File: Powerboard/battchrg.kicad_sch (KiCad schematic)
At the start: 60 parts, among them IC1 BQ24618RGET-iclr, J1 Thermistor Connection 103AT N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, J5 Conn_01x04_Male, J6 Conn_01x02_Male, J7 IsolationSwitch, Q1 RSJ250P10TL, Q2 RSJ250P10TL, Q3 RSJ250P10TL, Q4 RS1G120MN, Q5 RS1G120MN

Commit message: 3v3 reg cap & inductor changes, added boost capacitor
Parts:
- D1: footprint (none) -> Diode_SMD:D_SOT-23_ANK
- J7: footprint (none) -> Connector_AMASS:AMASS_XT60-M_1x02_P7.20mm_Vertical
- PackLED1, PowerLED1: footprint (none) -> LED_SMD:LED_0603_1608Metric
- TP16, TP17, TP18: footprint (none) -> TestPoint:TestPoint_Pad_D1.0mm
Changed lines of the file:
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@@
       (effects (font (size 1.27 1.27)) (justify left))
     )
-    (property "Footprint" "" (id 2) (at 246.38 96.52 90)
+    (property "Footprint" "Diode_SMD:D_SOT-23_ANK" (id 2) (at 246.38 96.52 90)
       (effects (font (size 1.27 1.27)) hide)
     )
@@
     (property "Reference" "PowerLED1" (id 0) (at 73.66 52.07 90))
     (property "Value" "LED" (id 1) (at 73.66 54.61 90))
-    (property "Footprint" "" (id 2) (at 67.31 53.34 0)
+    (property "Footprint" "LED_SMD:LED_0603_1608Metric" (id 2) (at 67.31 53.34 0)
       (effects (font (size 1.27 1.27)) hide)
     )
@@
       (effects (font (size 1.27 1.27)) (justify right))
     )
-    (property "Footprint" "" (id 2) (at 24.003 57.023 0)
+    (property "Footprint" "TestPoint:TestPoint_Pad_D1.0mm" (id 2) (at 24.003 57.023 0)
       (effects (font (size 1.27 1.27)) hide)
     )
@@
       (effects (font (size 1.27 1.27)) (justify left))
     )
-    (property "Footprint" "" (id 2) (at 69.85 182.118 0)
+    (property "Footprint" "TestPoint:TestPoint_Pad_D1.0mm" (id 2) (at 69.85 182.118 0)
       (effects (font (size 1.27 1.27)) hide)
     )
@@
       (effects (font (size 1.27 1.27)) (justify left))
     )
-    (property "Footprint" "" (id 2) (at 168.91 78.74 0)
+    (property "Footprint" "TestPoint:TestPoint_Pad_D1.0mm" (id 2) (at 168.91 78.74 0)
       (effects (font (size 1.27 1.27)) hide)
     )
@@
       (effects (font (size 1.27 1.27)) (justify left))
     )
-    (property "Footprint" "" (id 2) (at 74.93 170.18 0)
+    (property "Footprint" "Connector_AMASS:AMASS_XT60-M_1x02_P7.20mm_Vertical" (id 2) (at 74.93 170.18 0)
       (effects (font (size 1.27 1.27)) hide)
     )
@@
     (property "Reference" "PackLED1" (id 0) (at 64.77 134.62 0))
     (property "Value" "LED" (id 1) (at 64.77 139.7 0))
-    (property "Footprint" "" (id 2) (at 64.77 137.16 0)
-      (effects (font (size 1.27 1.27)) hide)
-    )
+    (property "Footprint" "LED_SMD:LED_0603_1608Metric" (id 2) (at 64.77 137.16 0)
+      (effects (font (size 1.27 1.27)) hide)
+    )

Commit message: assigned FPs for ceramic caps & most resistors
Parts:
- C1, C10, C11, C14, C15, C3, C31, C33, C4, C6: footprint (none) -> Capacitor_SMD:C_0603_1608Metric
- C32: footprint (none) -> Capacitor_SMD:C_1210_3225Metric
- IC1: footprint QFN50P400X400X100-25N-D -> (none)
- Q1, Q2, Q3: footprint RSJ151P10TL -> (none)
- R1, R10, R14, R15, R16, R17, R18, R2, R3, R5, R7, R9: footprint (none) -> Resistor_SMD:R_0603_1608Metric
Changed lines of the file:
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@@
     (property "Reference" "R16" (id 0) (at 191.77 119.38 90))
     (property "Value" "100Ω" (id 1) (at 191.77 121.92 90))
-    (property "Footprint" "" (id 2) (at 189.23 118.11 0)
+    (property "Footprint" "Resistor_SMD:R_0603_1608Metric" (id 2) (at 189.23 118.11 0)
       (effects (font (size 1.27 1.27)) hide)
     )
@@
       (effects (font (size 1.27 1.27)) (justify right))
     )
-    (property "Footprint" "" (id 2) (at 182.88 123.19 0)
+    (property "Footprint" "Resistor_SMD:R_0603_1608Metric" (id 2) (at 182.88 123.19 0)
       (effects (font (size 1.27 1.27)) hide)
     )
@@
       (effects (font (size 1.27 1.27)) (justify right))
     )
-    (property "Footprint" "" (id 2) (at 182.88 115.57 0)
+    (property "Footprint" "Resistor_SMD:R_0603_1608Metric" (id 2) (at 182.88 115.57 0)
       (effects (font (size 1.27 1.27)) hide)
     )
@@
       (effects (font (size 1.27 1.27)) (justify left))
     )
-    (property "Footprint" "" (id 2) (at 196.85 121.92 0)
+    (property "Footprint" "Capacitor_SMD:C_0603_1608Metric" (id 2) (at 196.85 121.92 0)
       (effects (font (size 1.27 1.27)) hide)
     )
@@
       (effects (font (size 1.27 1.27)) (justify left))
     )
-    (property "Footprint" "" (id 2) (at 239.522 135.89 90)
+    (property "Footprint" "Resistor_SMD:R_0603_1608Metric" (id 2) (at 239.522 135.89 90)
       (effects (font (size 1.27 1.27)) hide)
     )
@@
       (effects (font (size 1.27 1.27)) (justify left))
     )
-    (property "Footprint" "" (id 2) (at 252.222 135.89 90)
+    (property "Footprint" "Resistor_SMD:R_0603_1608Metric" (id 2) (at 252.222 135.89 90)
       (effects (font (size 1.27 1.27)) hide)
     )
@@
       (effects (font (size 1.27 1.27)) (justify left))
     )
-    (property "Footprint" "" (id 2) (at 245.872 135.89 90)
+    (property "Footprint" "Resistor_SMD:R_0603_1608Metric" (id 2) (at 245.872 135.89 90)
       (effects (font (size 1.27 1.27)) hide)
     )
@@
       (effects (font (size 1.27 1.27)) (justify left))
     )
-    (property "Footprint" "" (id 2) (at 203.2 102.87 0)
+    (property "Footprint" "Capacitor_SMD:C_0603_1608Metric" (id 2) (at 203.2 102.87 0)
       (effects (font (size 1.27 1.27)) hide)
     )
@@
       (effects (font (size 1.27 1.27)) (justify left))
     )
-    (property "Footprint" "" (id 2) (at 140.97 110.49 0)
+    (property "Footprint" "Resistor_SMD:R_0603_1608Metric" (id 2) (at 140.97 110.49 0)
       (effects (font (size 1.27 1.27)) hide)
     )
@@
       (effects (font (size 1.27 1.27)) (justify left))
     )
-    (property "Footprint" "" (id 2) (at 140.97 105.41 0)
+    (property "Footprint" "Capacitor_SMD:C_0603_1608Metric" (id 2) (at 140.97 105.41 0)
       (effects (font (size 1.27 1.27)) hide)
     )
@@
       (effects (font (size 1.27 1.27)) (justify left))
     )
-    (property "Footprint" "" (id 2) (at 132.08 107.95 0)
+    (property "Footprint" "Resistor_SMD:R_0603_1608Metric" (id 2) (at 132.08 107.95 0)
       (effects (font (size 1.27 1.27)) hide)
     )
@@
     (property "Reference" "R18" (id 0) (at 157.48 102.9716 90))
     (property "Value" "1kΩ" (id 1) (at 157.48 105.283 90))
-    (property "Footprint" "" (id 2) (at 157.48 107.95 0)
+    (property "Footprint" "Resistor_SMD:R_0603_1608Metric" (id 2) (at 157.48 107.95 0)
       (effects (font (size 1.27 1.27)) hide)
     )
@@
       (effects (font (size 1.27 1.27)) (justify left))
     )
-    (property "Footprint" "" (id 2) (at 252.73 115.57 0)
+    (property "Footprint" "Capacitor_SMD:C_0603_1608Metric" (id 2) (at 252.73 115.57 0)
       (effects (font (size 1.27 1.27)) hide)
     )
@@
       (effects (font (size 1.27 1.27)) (justify left))
     )
-    (property "Footprint" "" (id 2) (at 252.73 120.65 0)
+    (property "Footprint" "Capacitor_SMD:C_0603_1608Metric" (id 2) (at 252.73 120.65 0)
       (effects (font (size 1.27 1.27)) hide)
     )
@@
       (effects (font (size 1.27 1.27)) (justify left))
     )
-    (property "Footprint" "" (id 2) (at 198.12 63.5 0)
+    (property "Footprint" "Resistor_SMD:R_0603_1608Metric" (id 2) (at 198.12 63.5 0)
       (effects (font (size 1.27 1.27)) hide)
     )
@@
       (effects (font (size 1.27 1.27)) (justify left))
     )
-    (property "Footprint" "" (id 2) (at 198.12 67.31 0)
+    (property "Footprint" "Capacitor_SMD:C_0603_1608Metric" (id 2) (at 198.12 67.31 0)
       (effects (font (size 1.27 1.27)) hide)
     )
@@
       (effects (font (size 1.27 1.27)) (justify left))
     )
-    (property "Footprint" "" (id 2) (at 198.12 105.41 0)
+    (property "Footprint" "Capacitor_SMD:C_0603_1608Metric" (id 2) (at 198.12 105.41 0)
       (effects (font (size 1.27 1.27)) hide)
     )
@@
       (effects (font (size 1.27 1.27)) (justify left))
     )
-    (property "Footprint" "" (id 2) (at 199.39 110.49 0)
+    (property "Footprint" "Capacitor_SMD:C_0603_1608Metric" (id 2) (at 199.39 110.49 0)
       (effects (font (size 1.27 1.27)) hide)
     )
@@
     (property "Reference" "R2" (id 0) (at 55.88 119.38 90))
     (property "Value" "110kΩ" (id 1) (at 62.23 119.38 90))
-    (property "Footprint" "" (id 2) (at 58.42 121.92 0)
+    (property "Footprint" "Resistor_SMD:R_0603_1608Metric" (id 2) (at 58.42 121.92 0)
       (effects (font (size 1.27 1.27)) hide)
     )
@@
     (property "Reference" "R1" (id 0) (at 45.72 124.46 90))
     (property "Value" "10kΩ" (id 1) (at 45.72 129.54 90))
-    (property "Footprint" "" (id 2) (at 45.72 127 0)
+    (property "Footprint" "Resistor_SMD:R_0603_1608Metric" (id 2) (at 45.72 127 0)
       (effects (font (size 1.27 1.27)) hide)
     )
@@
       (effects (font (size 1.27 1.27)) (justify left))
     )
-    (property "Footprint" "" (id 2) (at 106.68 127 0)
+    (property "Footprint" "Capacitor_SMD:C_0603_1608Metric" (id 2) (at 106.68 127 0)
       (effects (font (size 1.27 1.27)) hide)
     )
@@
       (effects (font (size 1.27 1.27)) (justify left))
     )
-    (property "Footprint" "QFN50P400X400X100-25N-D" (id 2) (at 241.3 87.63 0)
+    (property "Footprint" "" (id 2) (at 241.3 87.63 0)
       (effects (font (size 1.27 1.27)) (justify left) hide)
     )
@@
     (property "Reference" "C31" (id 0) (at 108.1577 184.5801 90))
     (property "Value" "0.1μF" (id 1) (at 108.164 187.3161 90))
-    (property "Footprint" "" (id 2) (at 104.14 185.801 0)
+    (property "Footprint" "Capacitor_SMD:C_0603_1608Metric" (id 2) (at 104.14 185.801 0)
       (effects (font (size 1.27 1.27)) hide)
     )
@@
       (effects (font (size 1.27 1.27)) (justify left))
     )
-    (property "Footprint" "RSJ151P10TL" (id 2) (at 87.63 60.96 0)
+    (property "Footprint" "" (id 2) (at 87.63 60.96 0)
       (effects (font (size 1.27 1.27)) (justify left) hide)
     )
@@
       (effects (font (size 1.27 1.27)) (justify left))
     )
-    (property "Footprint" "RSJ151P10TL" (id 2) (at 215.9 45.72 0)
+    (property "Footprint" "" (id 2) (at 215.9 45.72 0)
       (effects (font (size 1.27 1.27)) (justify left) hide)
     )
@@
     (property "Reference" "C32" (id 0) (at 104.394 192.786 90))
     (property "Value" "22μF" (id 1) (at 104.267 194.818 90))
-    (property "Footprint" "" (id 2) (at 104.14 189.992 0)
+    (property "Footprint" "Capacitor_SMD:C_1210_3225Metric" (id 2) (at 104.14 189.992 0)
       (effects (font (size 1.27 1.27)) hide)
     )
@@
       (effects (font (size 1.27 1.27)) (justify left))
     )
-    (property "Footprint" "RSJ151P10TL" (id 2) (at 173.99 90.17 0)
-      (effects (font (size 1.27 1.27)) (justify left) hide)
-    )
+    (property "Footprint" "" (id 2) (at 173.99 90.17 0)
+      (effects (font (size 1.27 1.27)) (justify left) hide)
+    )

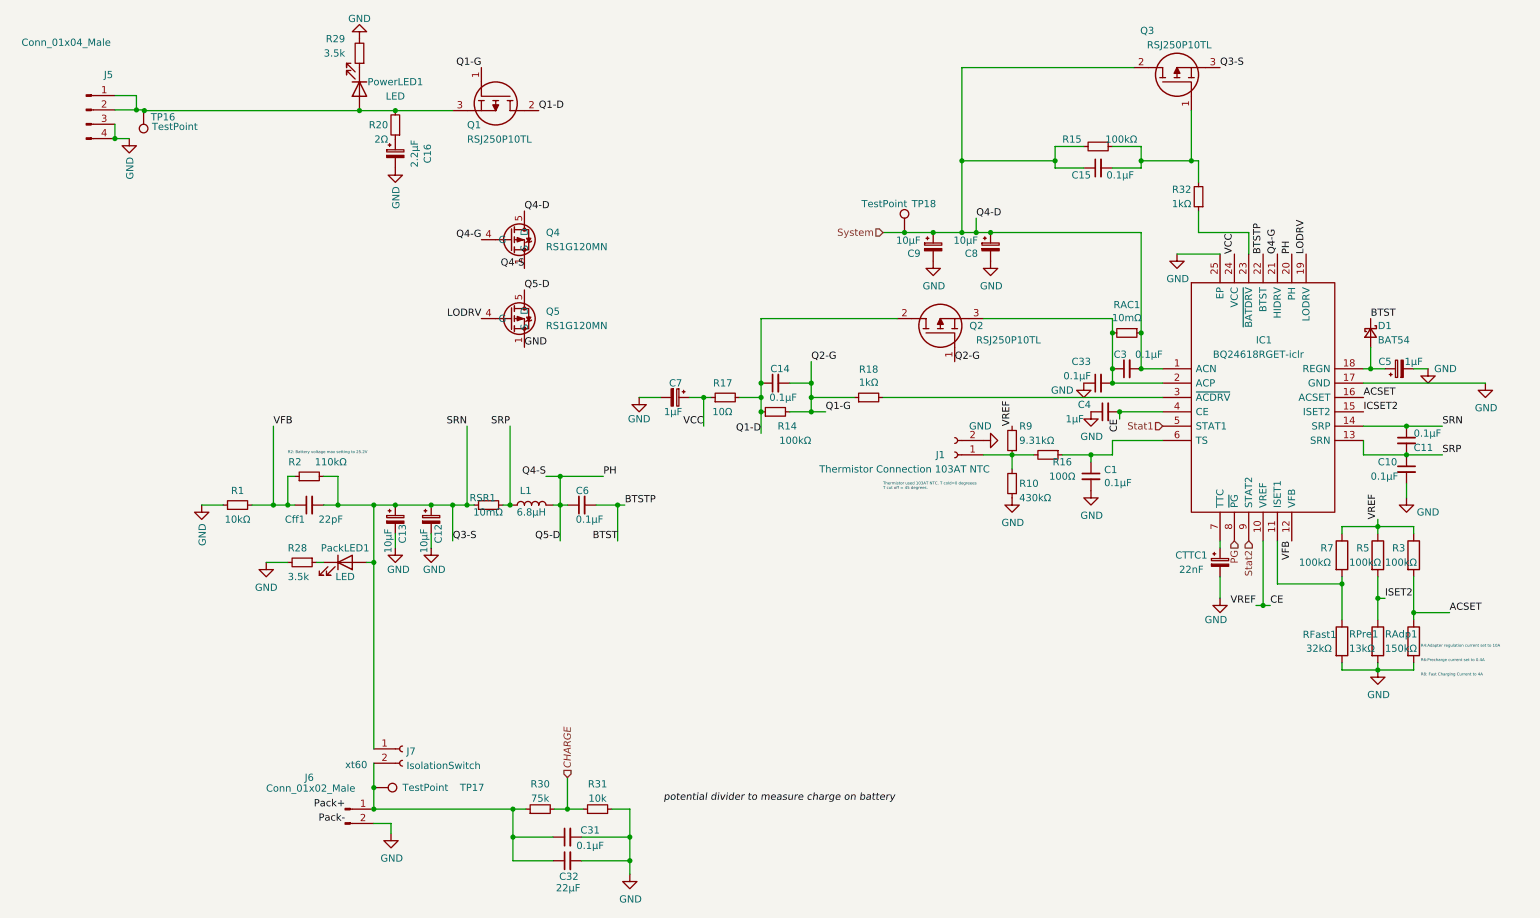
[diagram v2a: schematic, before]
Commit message: added components spreadsheet, changed some caps to ceramic
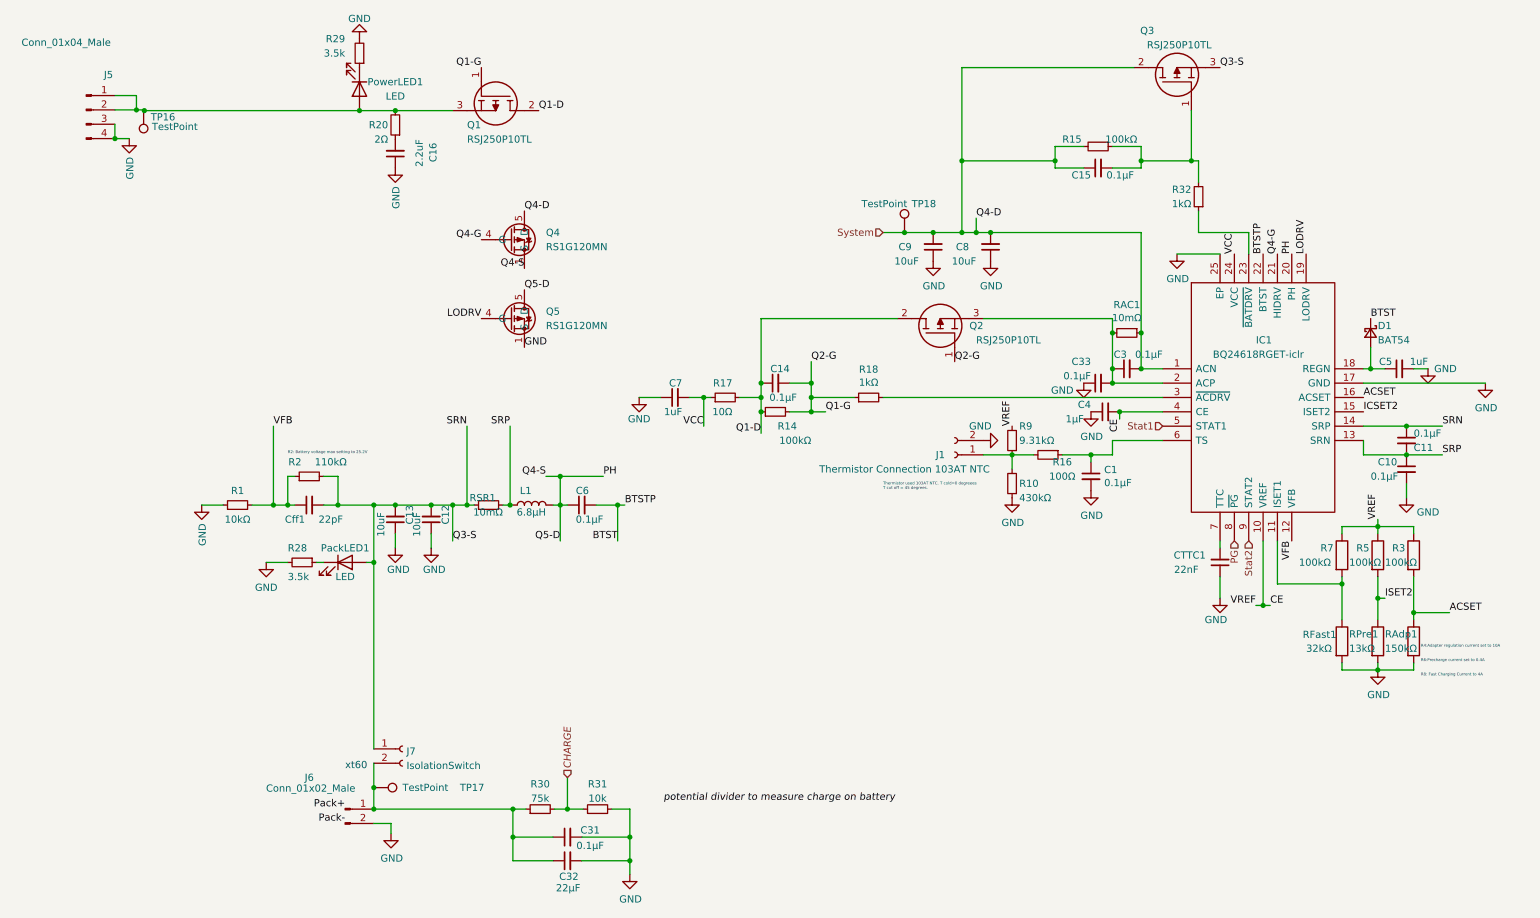
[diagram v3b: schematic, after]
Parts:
- removed C12, C13, C8, C9: 10μF, symbol Device:CP_Small
- removed C16: 2.2μF, symbol Device:CP_Small
- removed C5: 1μF, symbol Device:CP_Small
- removed C7: 1µF, symbol Device:CP_Small
- removed CTTC1: 22nF, symbol Device:CP_Small
- added C12, C13, C8, C9: 10uF, Capacitor_SMD:C_0603_1608Metric, symbol Device:C_Small
- added C16: 2.2uF, Capacitor_SMD:C_0603_1608Metric, symbol Device:C_Small
- added C5, C7: 1uF, Capacitor_SMD:C_0603_1608Metric, symbol Device:C_Small
- added CTTC1: 22nF, Capacitor_SMD:C_0603_1608Metric, symbol Device:C_Small
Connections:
- net GND: now also C12.1, C13.1, C16.1, C5.2, C7.1, C8.1, C9.1, CTTC1.1
- net Q3-S: now also C12.2, C13.2
- net System: now also C8.2, C9.2
- net VCC: now also C7.2
- net at D1.2 (A), IC1.18 (REGN): now also C5.1
- net at R20.1: now also C16.2
- net at IC1.7 (TTC): now also CTTC1.2

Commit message: actually changed caps this time
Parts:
- C12, C13, C16, C5, C7, C8, C9, CTTC1: footprint Capacitor_SMD:C_0603_1608Metric -> (none)
- Cff1: footprint (none) -> Capacitor_SMD:C_0603_1608Metric
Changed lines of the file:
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@@
     (property "Reference" "Cff1" (id 0) (at 55.88 129.54 90))
     (property "Value" "22pF" (id 1) (at 62.23 129.54 90))
-    (property "Footprint" "" (id 2) (at 58.42 127 0)
+    (property "Footprint" "Capacitor_SMD:C_0603_1608Metric" (id 2) (at 58.42 127 0)
       (effects (font (size 1.27 1.27)) hide)
     )
@@
       (effects (font (size 1.27 1.27)) (justify left))
     )
-    (property "Footprint" "Capacitor_SMD:C_0603_1608Metric" (id 2) (at 123.19 107.95 0)
+    (property "Footprint" "" (id 2) (at 123.19 107.95 0)
       (effects (font (size 1.27 1.27)) hide)
     )
@@
       (effects (font (size 1.27 1.27)) (justify left))
     )
-    (property "Footprint" "Capacitor_SMD:C_0603_1608Metric" (id 2) (at 168.91 81.28 0)
+    (property "Footprint" "" (id 2) (at 168.91 81.28 0)
       (effects (font (size 1.27 1.27)) hide)
     )
@@
       (effects (font (size 1.27 1.27)) (justify left))
     )
-    (property "Footprint" "Capacitor_SMD:C_0603_1608Metric" (id 2) (at 80.01 129.54 0)
+    (property "Footprint" "" (id 2) (at 80.01 129.54 0)
       (effects (font (size 1.27 1.27)) hide)
     )
@@
       (effects (font (size 1.27 1.27)) (justify left))
     )
-    (property "Footprint" "Capacitor_SMD:C_0603_1608Metric" (id 2) (at 219.71 137.16 0)
+    (property "Footprint" "" (id 2) (at 219.71 137.16 0)
       (effects (font (size 1.27 1.27)) hide)
     )
@@
       (effects (font (size 1.27 1.27)) (justify left))
     )
-    (property "Footprint" "Capacitor_SMD:C_0603_1608Metric" (id 2) (at 73.66 129.54 0)
+    (property "Footprint" "" (id 2) (at 73.66 129.54 0)
       (effects (font (size 1.27 1.27)) hide)
     )
@@
       (effects (font (size 1.27 1.27)) (justify left))
     )
-    (property "Footprint" "Capacitor_SMD:C_0603_1608Metric" (id 2) (at 73.66 64.77 0)
+    (property "Footprint" "" (id 2) (at 73.66 64.77 0)
       (effects (font (size 1.27 1.27)) hide)
     )
@@
       (effects (font (size 1.27 1.27)) (justify left))
     )
-    (property "Footprint" "Capacitor_SMD:C_0603_1608Metric" (id 2) (at 251.46 102.87 0)
+    (property "Footprint" "" (id 2) (at 251.46 102.87 0)
       (effects (font (size 1.27 1.27)) hide)
     )
@@
       (effects (font (size 1.27 1.27)) (justify left))
     )
-    (property "Footprint" "Capacitor_SMD:C_0603_1608Metric" (id 2) (at 179.07 81.28 0)
-      (effects (font (size 1.27 1.27)) hide)
-    )
+    (property "Footprint" "" (id 2) (at 179.07 81.28 0)
+      (effects (font (size 1.27 1.27)) hide)
+    )
